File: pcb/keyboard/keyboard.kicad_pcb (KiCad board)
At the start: 2 copper layers, 144.8 x 113 mm, 71 parts, among them J1 RJ45-8pin, J2 sidebutton, J3 RJ45-8pin, SW1 RESET_SW, U1 Arduino_Pro_Micro

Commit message: place new key footprints
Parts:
- KEY1, KEY10, KEY11, KEY12, KEY13, KEY14, KEY15, KEY16, KEY17, KEY18, KEY19, KEY2, KEY20, KEY21, KEY22, KEY23, KEY24, KEY25, KEY26, KEY3, KEY4, KEY5, KEY6, KEY7, KEY8, KEY9: footprint 4x6t2:MX_ALPS_REV_1.0U -> 4x6t2:MX_ALPS_KH_u1.00
- moved KEY16 2.54 mm to (16.5, 72.4)
- moved KEY17 2.54 mm to (16.5, 91.4)
- moved KEY18 2.54 mm to (16.5, 110.5)
- moved KEY15 2.54 mm to (16.5, 53.3)
- moved KEY1 0.09 mm to (95.2, 142.9)
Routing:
- net /ROW2: track 201.8 -> 0.00 mm, vias 1 -> 0
- net /ROW4: track 167.3 -> 0.00 mm, vias 1 -> 0
- net /COL6: track 165.7 -> 0.00 mm
- net /COL4: track 147.0 -> 0.00 mm
- net /COL5: track 145.1 -> 0.00 mm
- net /ROW1: track 128.9 -> 0.00 mm
- net /COL3: track 123.5 -> 0.00 mm
- net /ROW0: track 122.7 -> 0.00 mm
- net GND: track 114.4 -> 0.00 mm, vias 1 -> 0
- net /COL2: track 103.9 -> 0.00 mm
- net /COL0: track 80.2 -> 0.00 mm
- net /COL1: track 79.8 -> 0.00 mm
- net +5V: track 72.7 -> 0.00 mm
- net /RST: track 68.0 -> 0.00 mm
- net /SDA: track 63.3 -> 0.00 mm
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
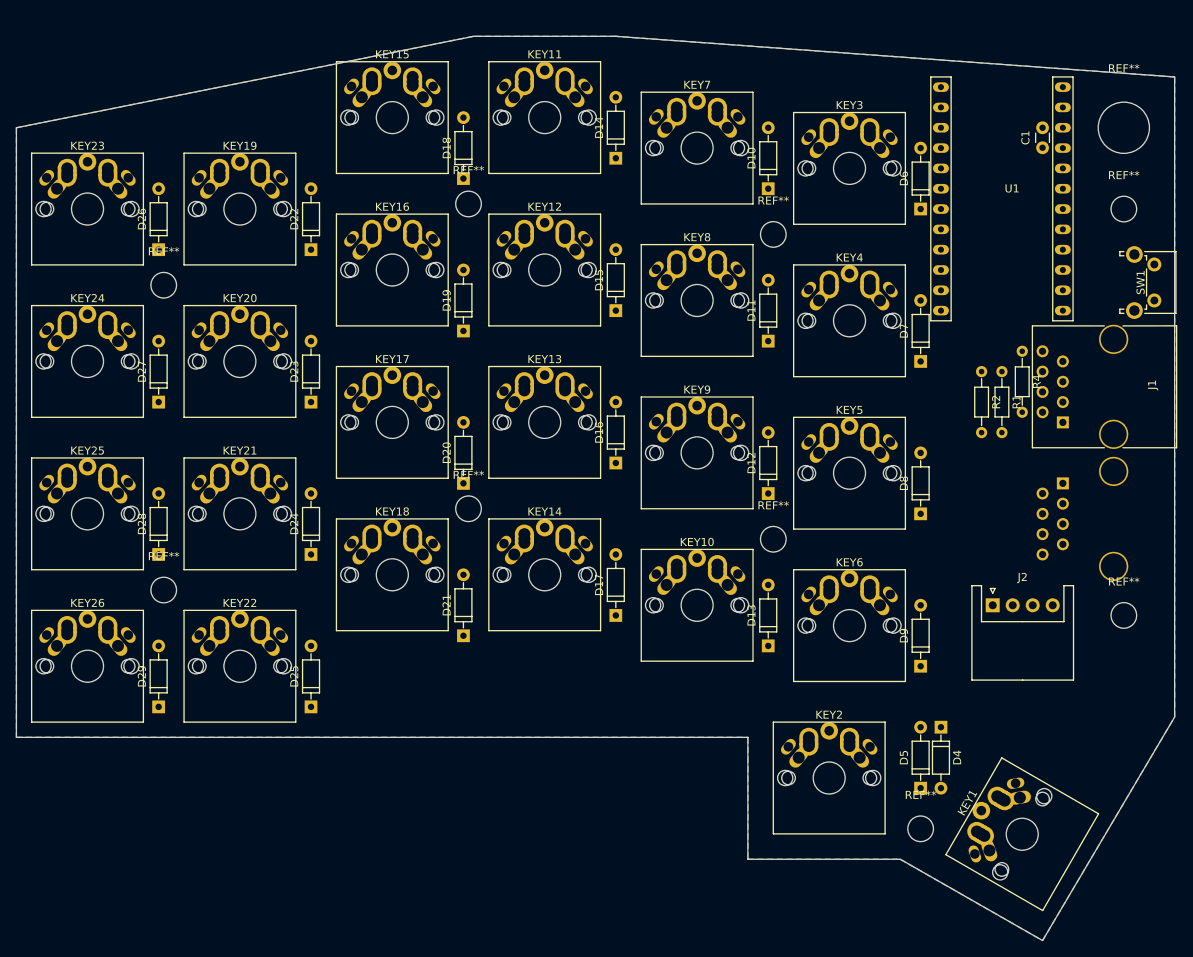
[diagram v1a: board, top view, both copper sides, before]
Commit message: tweak little finger key position
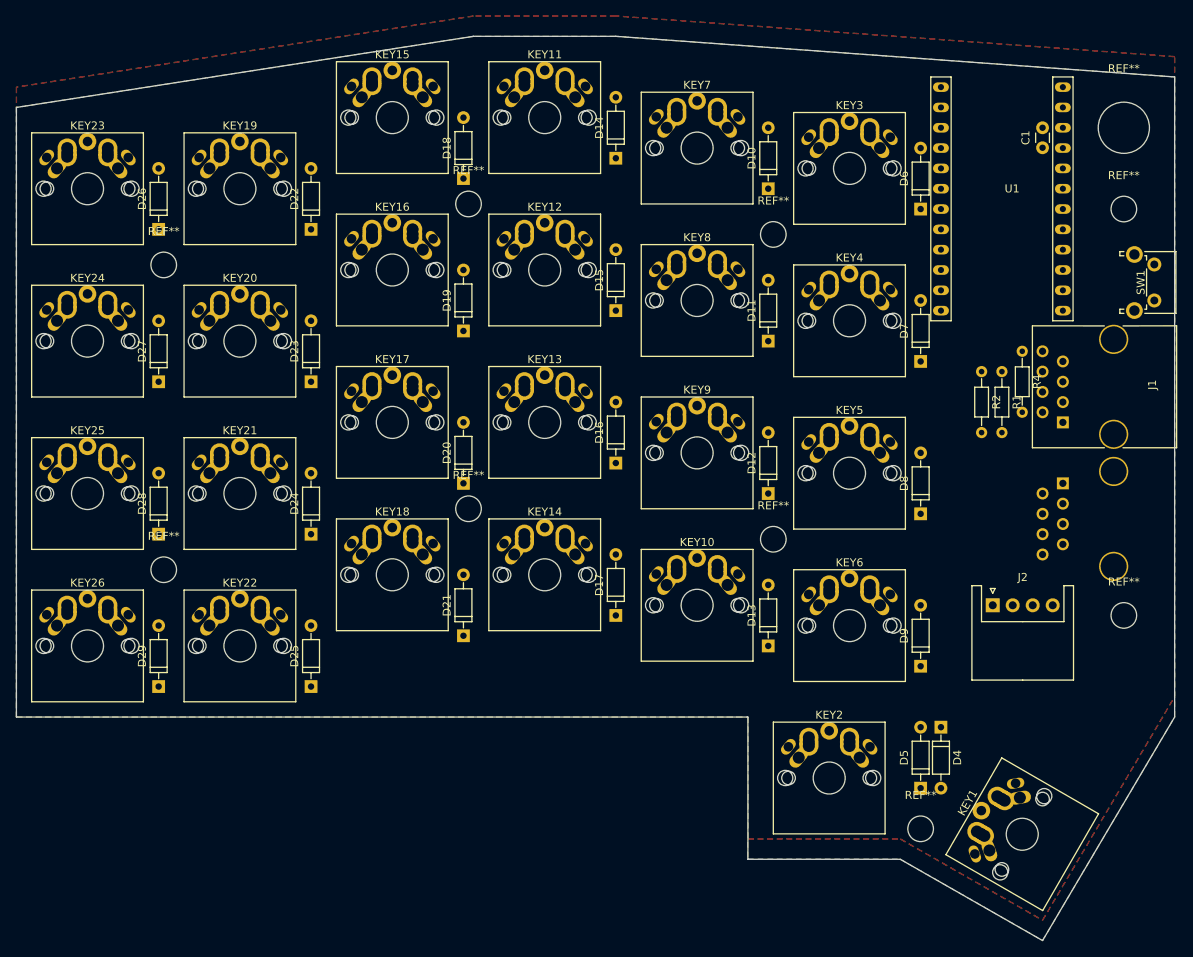
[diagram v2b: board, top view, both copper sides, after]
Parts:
- moved D23 2.54 mm to (6.35, 86.4)
- moved D24 2.54 mm to (6.35, 105.4)
- moved D25 2.54 mm to (6.35, 124.5)
- moved D27 2.54 mm to (-12.7, 86.4)
- moved D28 2.54 mm to (-12.7, 105.4)
- moved D29 2.54 mm to (-12.7, 124.5)
- moved KEY21 2.54 mm to (-2.54, 100.3)
- moved KEY22 2.54 mm to (-2.54, 119.4)
- moved KEY25 2.54 mm to (-21.6, 100.3)
- moved KEY26 2.54 mm to (-21.6, 119.4)
- moved REF** 2.54 mm to (-12.1, 71.8)
- moved KEY19 2.54 mm to (-2.54, 62.2)
- moved KEY23 2.54 mm to (-21.6, 62.2)
- moved D22 2.54 mm to (6.35, 67.3)
- moved D26 2.54 mm to (-12.7, 67.3)
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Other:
- outline, holes or cut-outs redrawn
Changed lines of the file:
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@@
   )
   (module Diodes_THT:D_DO-35_SOD27_P7.62mm_Horizontal (layer F.Cu)
-    (at 6.35 69.85 90)
+    (at 6.35 67.31 90)
     (descr "D, DO-35_SOD27 series, Axial, Horizontal, pin pitch=7.62mm, , length*diameter=4*2mm^2, , http://www.diodes.com/_files/packages/DO-35.pdf")
     (tags "D DO-35_SOD27 series Axial Horizontal pin pitch 7.62mm  length 4mm diameter 2mm")
@@
   )
   (module Diodes_THT:D_DO-35_SOD27_P7.62mm_Horizontal (layer F.Cu)
-    (at 6.35 88.9 90)
+    (at 6.35 86.36 90)
     (descr "D, DO-35_SOD27 series, Axial, Horizontal, pin pitch=7.62mm, , length*diameter=4*2mm^2, , http://www.diodes.com/_files/packages/DO-35.pdf")
     (tags "D DO-35_SOD27 series Axial Horizontal pin pitch 7.62mm  length 4mm diameter 2mm")
@@
   )
   (module Diodes_THT:D_DO-35_SOD27_P7.62mm_Horizontal (layer F.Cu)
-    (at 6.35 107.95 90)
+    (at 6.35 105.41 90)
     (descr "D, DO-35_SOD27 series, Axial, Horizontal, pin pitch=7.62mm, , length*diameter=4*2mm^2, , http://www.diodes.com/_files/packages/DO-35.pdf")
     (tags "D DO-35_SOD27 series Axial Horizontal pin pitch 7.62mm  length 4mm diameter 2mm")
@@
   )
   (module Diodes_THT:D_DO-35_SOD27_P7.62mm_Horizontal (layer F.Cu)
-    (at 6.35 127 90)
+    (at 6.35 124.46 90)
     (descr "D, DO-35_SOD27 series, Axial, Horizontal, pin pitch=7.62mm, , length*diameter=4*2mm^2, , http://www.diodes.com/_files/packages/DO-35.pdf")
     (tags "D DO-35_SOD27 series Axial Horizontal pin pitch 7.62mm  length 4mm diameter 2mm")
@@
   )
   (module Diodes_THT:D_DO-35_SOD27_P7.62mm_Horizontal (layer F.Cu)
-    (at -12.7 69.85 90)
+    (at -12.7 67.31 90)
     (descr "D, DO-35_SOD27 series, Axial, Horizontal, pin pitch=7.62mm, , length*diameter=4*2mm^2, , http://www.diodes.com/_files/packages/DO-35.pdf")
     (tags "D DO-35_SOD27 series Axial Horizontal pin pitch 7.62mm  length 4mm diameter 2mm")
@@
   )
   (module Diodes_THT:D_DO-35_SOD27_P7.62mm_Horizontal (layer F.Cu)
-    (at -12.7 88.9 90)
+    (at -12.7 86.36 90)
     (descr "D, DO-35_SOD27 series, Axial, Horizontal, pin pitch=7.62mm, , length*diameter=4*2mm^2, , http://www.diodes.com/_files/packages/DO-35.pdf")
     (tags "D DO-35_SOD27 series Axial Horizontal pin pitch 7.62mm  length 4mm diameter 2mm")
@@
   )
   (module Diodes_THT:D_DO-35_SOD27_P7.62mm_Horizontal (layer F.Cu)
-    (at -12.7 107.95 90)
+    (at -12.7 105.41 90)
     (descr "D, DO-35_SOD27 series, Axial, Horizontal, pin pitch=7.62mm, , length*diameter=4*2mm^2, , http://www.diodes.com/_files/packages/DO-35.pdf")
     (tags "D DO-35_SOD27 series Axial Horizontal pin pitch 7.62mm  length 4mm diameter 2mm")
@@
   )
   (module Diodes_THT:D_DO-35_SOD27_P7.62mm_Horizontal (layer F.Cu)
-    (at -12.7 127 90)
+    (at -12.7 124.46 90)
     (descr "D, DO-35_SOD27 series, Axial, Horizontal, pin pitch=7.62mm, , length*diameter=4*2mm^2, , http://www.diodes.com/_files/packages/DO-35.pdf")
     (tags "D DO-35_SOD27 series Axial Horizontal pin pitch 7.62mm  length 4mm diameter 2mm")
@@
   )
   (module Mounting_Holes:MountingHole_3.2mm_M3 (layer F.Cu)
-    (at -12.065 74.295)
+    (at -12.065 71.755)
     (descr "Mounting Hole 3.2mm, no annular, M3")
     (tags "mounting hole 3.2mm no annular m3")
@@
   )
   (module Mounting_Holes:MountingHole_3.2mm_M3 (layer F.Cu)
-    (at -12.065 112.395)
+    (at -12.065 109.855)
     (descr "Mounting Hole 3.2mm, no annular, M3")
     (tags "mounting hole 3.2mm no annular m3")
@@
   )
   (module 4x6t2:MX_ALPS_KH_u1.00 (layer F.Cu)
-    (at -21.59 64.77)
+    (at -21.59 62.23)
     (descr "Cherry MX keyswitch, MX1A, 1u, PCB mount, http://cherryamericas.com/wp-content/uploads/2014/12/mx_cat.pdf")
     (tags "cherry mx keyswitch MX1A 1u PCB")
@@
   )
   (module 4x6t2:MX_ALPS_KH_u1.00 (layer F.Cu)
-    (at -21.59 83.82)
+    (at -21.59 81.28)
     (descr "Cherry MX keyswitch, MX1A, 1u, PCB mount, http://cherryamericas.com/wp-content/uploads/2014/12/mx_cat.pdf")
     (tags "cherry mx keyswitch MX1A 1u PCB")
@@
   )
   (module 4x6t2:MX_ALPS_KH_u1.00 (layer F.Cu)
-    (at -21.59 102.87)
+    (at -21.59 100.33)
     (descr "Cherry MX keyswitch, MX1A, 1u, PCB mount, http://cherryamericas.com/wp-content/uploads/2014/12/mx_cat.pdf")
     (tags "cherry mx keyswitch MX1A 1u PCB")
@@
   )
   (module 4x6t2:MX_ALPS_KH_u1.00 (layer F.Cu)
-    (at -21.59 121.92)
+    (at -21.59 119.38)
     (descr "Cherry MX keyswitch, MX1A, 1u, PCB mount, http://cherryamericas.com/wp-content/uploads/2014/12/mx_cat.pdf")
     (tags "cherry mx keyswitch MX1A 1u PCB")
@@
   )
   (module 4x6t2:MX_ALPS_KH_u1.00 (layer F.Cu)
-    (at -2.54 64.77)
+    (at -2.54 62.23)
     (descr "Cherry MX keyswitch, MX1A, 1u, PCB mount, http://cherryamericas.com/wp-content/uploads/2014/12/mx_cat.pdf")
     (tags "cherry mx keyswitch MX1A 1u PCB")
@@
   )
   (module 4x6t2:MX_ALPS_KH_u1.00 (layer F.Cu)
-    (at -2.54 83.82)
+    (at -2.54 81.28)
     (descr "Cherry MX keyswitch, MX1A, 1u, PCB mount, http://cherryamericas.com/wp-content/uploads/2014/12/mx_cat.pdf")
     (tags "cherry mx keyswitch MX1A 1u PCB")
@@
   )
   (module 4x6t2:MX_ALPS_KH_u1.00 (layer F.Cu)
-    (at -2.54 102.87)
+    (at -2.54 100.33)
     (descr "Cherry MX keyswitch, MX1A, 1u, PCB mount, http://cherryamericas.com/wp-content/uploads/2014/12/mx_cat.pdf")
     (tags "cherry mx keyswitch MX1A 1u PCB")
@@
   )
   (module 4x6t2:MX_ALPS_KH_u1.00 (layer F.Cu)
-    (at -2.54 121.92)
+    (at -2.54 119.38)
     (descr "Cherry MX keyswitch, MX1A, 1u, PCB mount, http://cherryamericas.com/wp-content/uploads/2014/12/mx_cat.pdf")
     (tags "cherry mx keyswitch MX1A 1u PCB")
@@
   (gr_line (start 80.01 146.05) (end 97.79 156.21) (layer Edge.Cuts) (width 0.1))
   (gr_line (start 60.96 146.05) (end 80.01 146.05) (layer Edge.Cuts) (width 0.1))
-  (gr_line (start 60.96 130.81) (end 60.96 146.05) (layer Edge.Cuts) (width 0.1))
-  (gr_line (start -30.48 130.81) (end 60.96 130.81) (layer Edge.Cuts) (width 0.1))
-  (gr_line (start -30.48 54.61) (end -30.48 130.81) (layer Edge.Cuts) (width 0.1))
-  (gr_line (start 26.67 43.18) (end -30.48 54.61) (layer Edge.Cuts) (width 0.1))
+  (gr_line (start 60.96 128.27) (end 60.96 146.05) (layer Edge.Cuts) (width 0.1))
+  (gr_line (start -30.48 128.27) (end 60.96 128.27) (layer Edge.Cuts) (width 0.1))
+  (gr_line (start -30.48 52.07) (end -30.48 128.27) (layer Edge.Cuts) (width 0.1))
+  (gr_line (start 26.67 43.18) (end -30.48 52.07) (layer Edge.Cuts) (width 0.1))
   (gr_line (start 44.45 43.18) (end 26.67 43.18) (layer Edge.Cuts) (width 0.1))
   (gr_line (start 114.3 48.26) (end 44.45 43.18) (layer Edge.Cuts) (width 0.1))
@@
     (polygon
       (pts
-        (xy 114.3 48.26) (xy 44.45 43.18) (xy 26.67 43.18) (xy -30.48 54.61) (xy -30.48 130.81)
-        (xy 60.96 130.81) (xy 60.96 146.05) (xy 80.01 146.05) (xy 97.79 156.21) (xy 114.3 128.27)
-        (xy 114.3 128.27)
+        (xy 114.3 45.72) (xy 44.45 40.64) (xy 26.67 40.64) (xy -30.48 49.53) (xy -30.48 128.27)
+        (xy 60.96 128.27) (xy 60.96 143.51) (xy 80.01 143.51) (xy 97.79 153.67) (xy 114.3 125.73)
+        (xy 114.3 125.73)
       )
     )
@@
     (polygon
       (pts
-        (xy 114.3 128.27) (xy 114.3 48.26) (xy 44.45 43.18) (xy 26.67 43.18) (xy -30.48 54.61)
-        (xy -30.48 130.81) (xy 60.96 130.81) (xy 60.96 146.05) (xy 80.01 146.05) (xy 97.79 156.21)
+        (xy 114.3 128.27) (xy 114.3 48.26) (xy 44.45 43.18) (xy 26.67 43.18) (xy -30.48 52.07)
+        (xy -30.48 128.27) (xy 60.96 128.27) (xy 60.96 146.05) (xy 80.01 146.05) (xy 97.79 156.21)
       )
     )

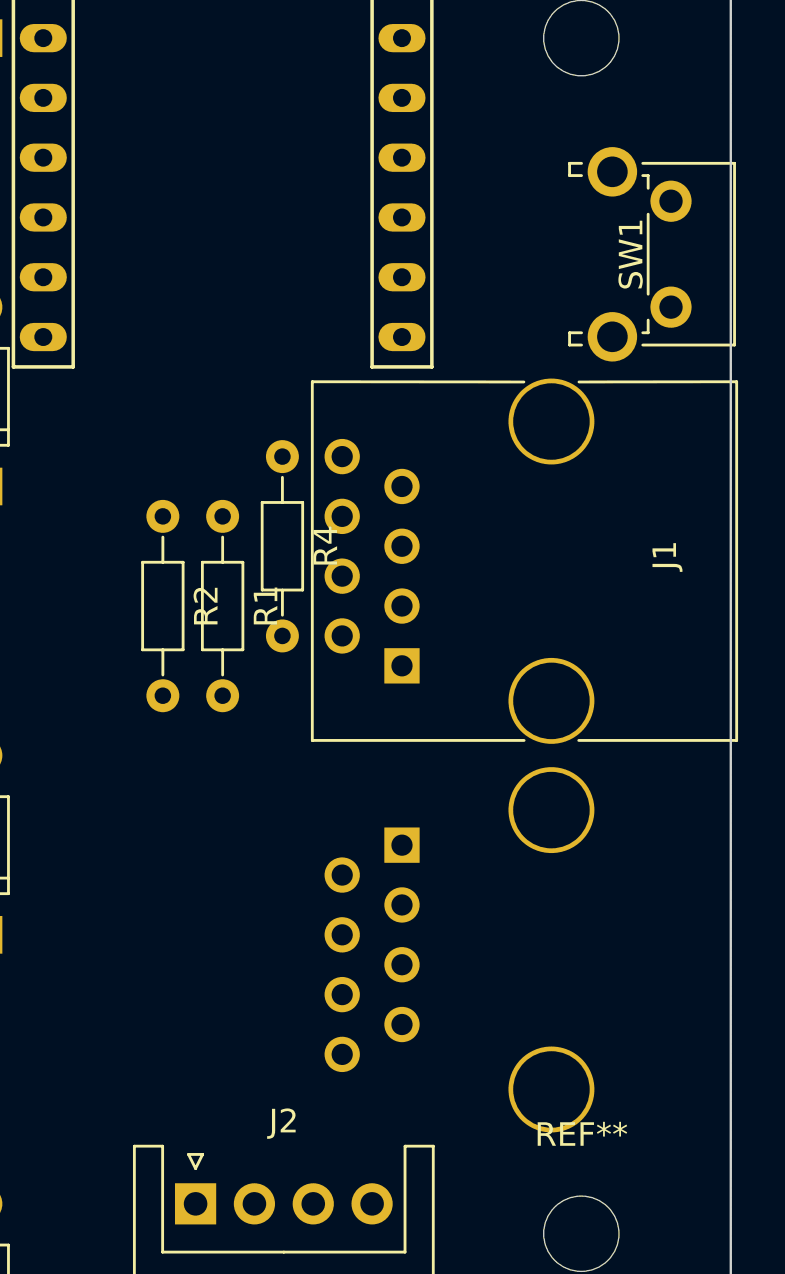
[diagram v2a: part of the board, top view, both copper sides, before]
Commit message: RJ45 -> Audio Jack 4pin
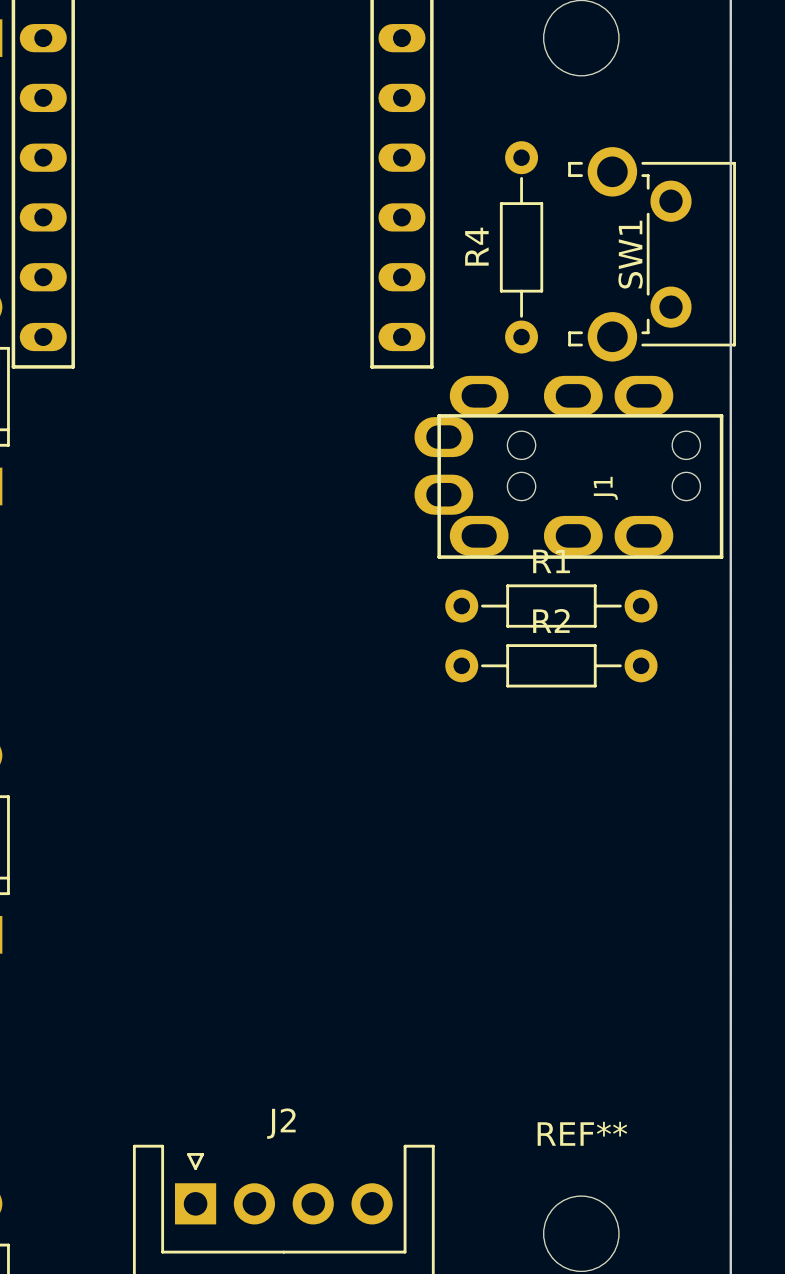
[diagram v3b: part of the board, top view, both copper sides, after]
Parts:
- removed J3: RJ45-8pin, Connectors:RJ45_8
- J1: value RJ45-8pin -> Audio-Jack-4; footprint Connectors:RJ45_8 -> 4x6t2:MJ-4PP-9_rev2
- moved J1 15.6 mm to (113.9, 83.8), turned to 270 degrees
- moved R2 14.2 mm to (102.9, 91.4), turned to 0 degrees
- moved R4 11.4 mm to (105.4, 77.5), turned to 90 degrees
- moved R1 10.9 mm to (102.9, 88.9), turned to 0 degrees
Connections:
- J1 pad 1: GND -> /SCL
- J1 pad 2: GND -> /SDA
- J1 pad 3: GND -> +5V

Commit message: wiring
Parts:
- moved J2 20.5 mm to (101.7, 96.5)
- moved KEY16 2.54 mm to (16.5, 74.9)
- moved KEY17 2.54 mm to (16.5, 94.0)
- moved KEY18 2.54 mm to (16.5, 113.0)
- moved KEY15 2.54 mm to (16.5, 55.9)
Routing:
- net /ROW2: track 0.00 -> 262.5 mm
- net /ROW4: track 0.00 -> 221.8 mm, vias 0 -> 1
- net /COL4: track 0.00 -> 181.6 mm, vias 0 -> 1
- net /ROW1: track 0.00 -> 175.6 mm
- net /COL6: track 0.00 -> 168.7 mm, vias 0 -> 8
- net /COL3: track 0.00 -> 164.2 mm, vias 0 -> 1
- net /ROW0: track 0.00 -> 155.2 mm
- net /COL5: track 0.00 -> 144.0 mm, vias 0 -> 6
- net /COL2: track 0.00 -> 143.3 mm, vias 0 -> 1
- net /COL1: track 0.00 -> 84.6 mm, vias 0 -> 2
- net /COL0: track 0.00 -> 77.2 mm
- net GND: track 0.00 -> 70.1 mm
- net +5V: track 0.00 -> 53.4 mm
- net /Y: track 0.00 -> 40.9 mm
- net /SDA: track 0.00 -> 38.2 mm
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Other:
- rule trace_min: 0 -> 0.2032
